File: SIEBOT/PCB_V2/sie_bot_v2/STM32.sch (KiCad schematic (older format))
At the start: 50 parts, among them P11 CONN_3X2, P12 CONN_3X2, P13 CONN_3X2, P14 CONN_3X2, P8 CONN_12X2, P9 CONN_12X2, Q2 BS170F, Q3 BS170F, Q4 BS170F, Q5 BS170F, Q6 BS170F, Q7 BS170F, Q8 BS170F, Q9 BS170F, U10 STM32F105RC, U11 LT1117CST-3.3, U12 ZXMHC3F381N8, U13 ZXMHC3F381N8, U14 ZXMHC3F381N8, U15 ZXMHC3F381N8, X3 8MHz

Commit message: Adición de ejemplos, modificación de los fuentes de elua para soportar el stm32f105
Cambios en el PCB para tener comunicación entre el IMX y el STM32 por puerto serial e i2c
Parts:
- removed P11, P12, P13, P14: CONN_3X2, pin_array_3x2, symbol CONN_3X2
- removed R26: 510, SM0603, symbol R
- added P?: CONN_5X2, pin_array_5x2, symbol CONN_5X2
- added R46: 150, SM0603, symbol R
- added R? (x2): 4.7k, SM0603, symbol R
- X3: value 8MHz -> 12MHz; footprint ABM3B -> ABM8G
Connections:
- net labels added: GMTR, STM_UART_RX, STM_UART_TX, VMTR
- net labels removed: GMTR1, GMTR2, GMTR3, GMTR4, VMTR1, VMTR2, VMTR3, VMTR4
- wire segments 266 -> 259
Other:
- note removed: "Boot mode select"
- note removed: "El procesador selecciona si inicia por \nla flash o ram internas.\nSe debe soldar solo R26 o R34\n\n"
- moved on the sheet: R34, R40, R41, R44, R45, U14, U15

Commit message: Inicio de ruteo de los cambios realizados en el esquematico
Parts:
- P6: renamed from P?; footprint pin_array_5x2 -> PIN_ARRAY_5x2
- gave numbers to parts that had none: 2
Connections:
- net labels added: TDO
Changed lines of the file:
@@
-EESchema Schematic File Version 2  date Fri 10 Feb 2012 05:02:18 PM COT
+EESchema Schematic File Version 2  date Fri 10 Feb 2012 06:23:52 PM COT
 LIBS:con-jack
 LIBS:adm3101e
@@
 STM_UART_RX
 $Comp
-L R R?
+L R R47
 U 1 1 4F352DAA
 P 2050 7200
-F 0 "R?" V 2130 7200 50  0000 C CNN
+F 0 "R47" V 2130 7200 50  0000 C CNN
 F 1 "4.7k" V 2050 7200 50  0000 C CNN
 F 2 "SM0603" H 2050 7200 60  0001 C CNN
@@
 $EndComp
 $Comp
-L R R?
+L R R26
 U 1 1 4F352D8D
 P 1900 7200
-F 0 "R?" V 1980 7200 50  0000 C CNN
+F 0 "R26" V 1980 7200 50  0000 C CNN
 F 1 "4.7k" V 1900 7200 50  0000 C CNN
 F 2 "SM0603" H 1900 7200 60  0001 C CNN
@@
 $EndComp
 $Comp
-L 3V3 #PWR?
+L 3V3 #PWR80
 U 1 1 4F352D37
 P 2050 6850
-F 0 "#PWR?" H 2050 6950 30  0001 C CNN
+F 0 "#PWR80" H 2050 6950 30  0001 C CNN
 F 1 "3V3" H 2050 6960 30  0000 C CNN
 	1    2050 6850
@@
 VMTR
 $Comp
-L CONN_5X2 P?
+L CONN_5X2 P6
 U 1 1 4F352742
 P 9050 6200
-F 0 "P?" H 9050 6500 60  0000 C CNN
+F 0 "P6" H 9050 6500 60  0000 C CNN
 F 1 "CONN_5X2" V 9050 6200 50  0000 C CNN
-F 2 "pin_array_5x2" H 9050 6200 60  0001 C CNN
+F 2 "PIN_ARRAY_5x2" H 9050 6200 60  0001 C CNN
 	1    9050 6200
 	1    0    0    -1
@@
 I2C1_SDA
 $Comp
-L 3V3 #PWR8
+L 3V3 #PWR86
 U 1 1 4E8A099D
 P 6050 8950
-F 0 "#PWR8" H 6050 9050 30  0001 C CNN
+F 0 "#PWR86" H 6050 9050 30  0001 C CNN
 F 1 "3V3" H 6050 9060 30  0000 C CNN
 	1    6050 8950
@@
 $EndComp
 $Comp
-L 3V3 #PWR3
+L 3V3 #PWR81
 U 1 1 4E8A0997
 P 3700 7900
-F 0 "#PWR3" H 3700 8000 30  0001 C CNN
+F 0 "#PWR81" H 3700 8000 30  0001 C CNN
 F 1 "3V3" H 3700 8010 30  0000 C CNN
 	1    3700 7900
@@
 $EndComp
 $Comp
-L 3V3 #PWR2
+L 3V3 #PWR79
 U 1 1 4E8A0992
 P 1500 7900
-F 0 "#PWR2" H 1500 8000 30  0001 C CNN
+F 0 "#PWR79" H 1500 8000 30  0001 C CNN
 F 1 "3V3" H 1500 8010 30  0000 C CNN
 	1    1500 7900
@@
 $EndComp
 $Comp
-L VDD5V #PWR9
+L VDD5V #PWR083
 U 1 1 4E7B5061
 P 6700 1000
-F 0 "#PWR9" H 6700 1100 30  0001 C CNN
+F 0 "#PWR083" H 6700 1100 30  0001 C CNN
 F 1 "VDD5V" H 6700 1100 30  0000 C CNN
 	1    6700 1000
@@
 $EndComp
 $Comp
-L GND #PWR10
+L GND #PWR084
 U 1 1 4E7B4E89
 P 6700 1650
-F 0 "#PWR10" H 6700 1650 30  0001 C CNN
+F 0 "#PWR084" H 6700 1650 30  0001 C CNN
 F 1 "GND" H 6700 1580 30  0001 C CNN
 	1    6700 1650
@@
 $EndComp
 $Comp
-L GND #PWR14
+L GND #PWR085
 U 1 1 4E7B4E84
 P 8150 1650
-F 0 "#PWR14" H 8150 1650 30  0001 C CNN
+F 0 "#PWR085" H 8150 1650 30  0001 C CNN
 F 1 "GND" H 8150 1580 30  0001 C CNN
 	1    8150 1650
@@
 $EndComp
 $Comp
-L GND #PWR12
+L GND #PWR086
 U 1 1 4E7B44BE
 P 7750 1650
-F 0 "#PWR12" H 7750 1650 30  0001 C CNN
+F 0 "#PWR086" H 7750 1650 30  0001 C CNN
 F 1 "GND" H 7750 1580 30  0001 C CNN
 	1    7750 1650
@@
 $EndComp
 $Comp
-L GND #PWR11
+L GND #PWR087
 U 1 1 4E7B44A2
 P 6900 1250
-F 0 "#PWR11" H 6900 1250 30  0001 C CNN
+F 0 "#PWR087" H 6900 1250 30  0001 C CNN
 F 1 "GND" H 6900 1180 30  0001 C CNN
 	1    6900 1250
@@
 $EndComp
 $Comp
-L 3V3 #PWR13
+L 3V3 #PWR91
 U 1 1 4E7B4482
 P 8150 900
-F 0 "#PWR13" H 8150 1000 30  0001 C CNN
+F 0 "#PWR91" H 8150 1000 30  0001 C CNN
 F 1 "3V3" H 8150 1010 30  0000 C CNN
 	1    8150 900
@@
 $EndComp
 $Comp
-L GND #PWR24
+L GND #PWR088
 U 1 1 4E78C5F4
 P 10800 2850
-F 0 "#PWR24" H 10800 2850 30  0001 C CNN
+F 0 "#PWR088" H 10800 2850 30  0001 C CNN
 F 1 "GND" H 10800 2780 30  0001 C CNN
 	1    10800 2850
@@
 $EndComp
 $Comp
-L 3V3 #PWR16
+L 3V3 #PWR94
 U 1 1 4E78C319
 P 8550 2150
-F 0 "#PWR16" H 8550 2250 30  0001 C CNN
+F 0 "#PWR94" H 8550 2250 30  0001 C CNN
 F 1 "3V3" H 8550 2260 30  0000 C CNN
 	1    8550 2150
@@
 $EndComp
 $Comp
-L GND #PWR7
+L GND #PWR089
 U 1 1 4E78C2ED
 P 5300 7400
-F 0 "#PWR7" H 5300 7400 30  0001 C CNN
+F 0 "#PWR089" H 5300 7400 30  0001 C CNN
 F 1 "GND" H 5300 7330 30  0001 C CNN
 	1    5300 7400
@@
 JTDI
 $Comp
-L 3V3 #PWR4
+L 3V3 #PWR82
 U 1 1 4E78BA06
 P 4150 1100
-F 0 "#PWR4" H 4150 1200 30  0001 C CNN
+F 0 "#PWR82" H 4150 1200 30  0001 C CNN
 F 1 "3V3" H 4150 1210 30  0000 C CNN
 	1    4150 1100
@@
 $EndComp
 $Comp
-L 3V3 #PWR15
+L 3V3 #PWR93
 U 1 1 4E2A2E11
 P 8350 2150
-F 0 "#PWR15" H 8350 2250 30  0001 C CNN
+F 0 "#PWR93" H 8350 2250 30  0001 C CNN
 F 1 "3V3" H 8350 2260 30  0000 C CNN
 	1    8350 2150
@@
 $EndComp
 $Comp
-L 3V3 #PWR18
+L 3V3 #PWR96
 U 1 1 4E2A2E03
 P 8750 1000
-F 0 "#PWR18" H 8750 1100 30  0001 C CNN
+F 0 "#PWR96" H 8750 1100 30  0001 C CNN
 F 1 "3V3" H 8750 1110 30  0000 C CNN
 	1    8750 1000
@@
 $EndComp
 $Comp
-L 3V3 #PWR6
+L 3V3 #PWR84
 U 1 1 4E2A2DF0
 P 4700 1150
-F 0 "#PWR6" H 4700 1250 30  0001 C CNN
+F 0 "#PWR84" H 4700 1250 30  0001 C CNN
 F 1 "3V3" H 4700 1260 30  0000 C CNN
 	1    4700 1150
@@
 $EndComp
 $Comp
-L GND #PWR22
+L GND #PWR090
 U 1 1 4E188E4E
 P 10550 1500
-F 0 "#PWR22" H 10550 1500 30  0001 C CNN
+F 0 "#PWR090" H 10550 1500 30  0001 C CNN
 F 1 "GND" H 10550 1430 30  0001 C CNN
 	1    10550 1500
@@
 FP1
 $Comp
-L GND #PWR19
+L GND #PWR091
 U 1 1 4E186DEB
 P 9250 1500
-F 0 "#PWR19" H 9250 1500 30  0001 C CNN
+F 0 "#PWR091" H 9250 1500 30  0001 C CNN
 F 1 "GND" H 9250 1430 30  0001 C CNN
 	1    9250 1500
@@
 JTRST
 Text Label 6100 6300 2    60   ~ 0
-JTDO
+TDO
 Text Label 6100 6200 2    60   ~ 0
 JTMS
@@
 $EndComp
 $Comp
-L GND #PWR17
+L GND #PWR092
 U 1 1 4E07869F
 P 8550 2800
-F 0 "#PWR17" H 8550 2800 30  0001 C CNN
+F 0 "#PWR092" H 8550 2800 30  0001 C CNN
 F 1 "GND" H 8550 2730 30  0001 C CNN
 	1    8550 2800
@@
 $EndComp
 $Comp
-L GND #PWR5
+L GND #PWR093
 U 1 1 4DCDB18D
 P 4300 7400
-F 0 "#PWR5" H 4300 7400 30  0001 C CNN
+F 0 "#PWR093" H 4300 7400 30  0001 C CNN
 F 1 "GND" H 4300 7330 30  0001 C CNN
 	1    4300 7400
@@
 $EndComp
 $Comp
-L GND #PWR20
+L GND #PWR094
 U 1 1 4DCDB183
 P 9650 2800
-F 0 "#PWR20" H 9650 2800 30  0001 C CNN
+F 0 "#PWR094" H 9650 2800 30  0001 C CNN
 F 1 "GND" H 9650 2730 30  0001 C CNN
 	1    9650 2800
@@
 NRST
 $Comp
-L GND #PWR1
+L GND #PWR095
 U 1 1 4DCDB180
 P 700 2050
-F 0 "#PWR1" H 700 2050 30  0001 C CNN
+F 0 "#PWR095" H 700 2050 30  0001 C CNN
 F 1 "GND" H 700 1980 30  0001 C CNN
 	1    700  2050
@@
 BOOT0
 $Comp
-L GND #PWR21
+L GND #PWR096
 U 1 1 4DCDB17D
 P 10400 2850
-F 0 "#PWR21" H 10400 2850 30  0001 C CNN
+F 0 "#PWR096" H 10400 2850 30  0001 C CNN
 F 1 "GND" H 10400 2780 30  0001 C CNN
 	1    10400 2850

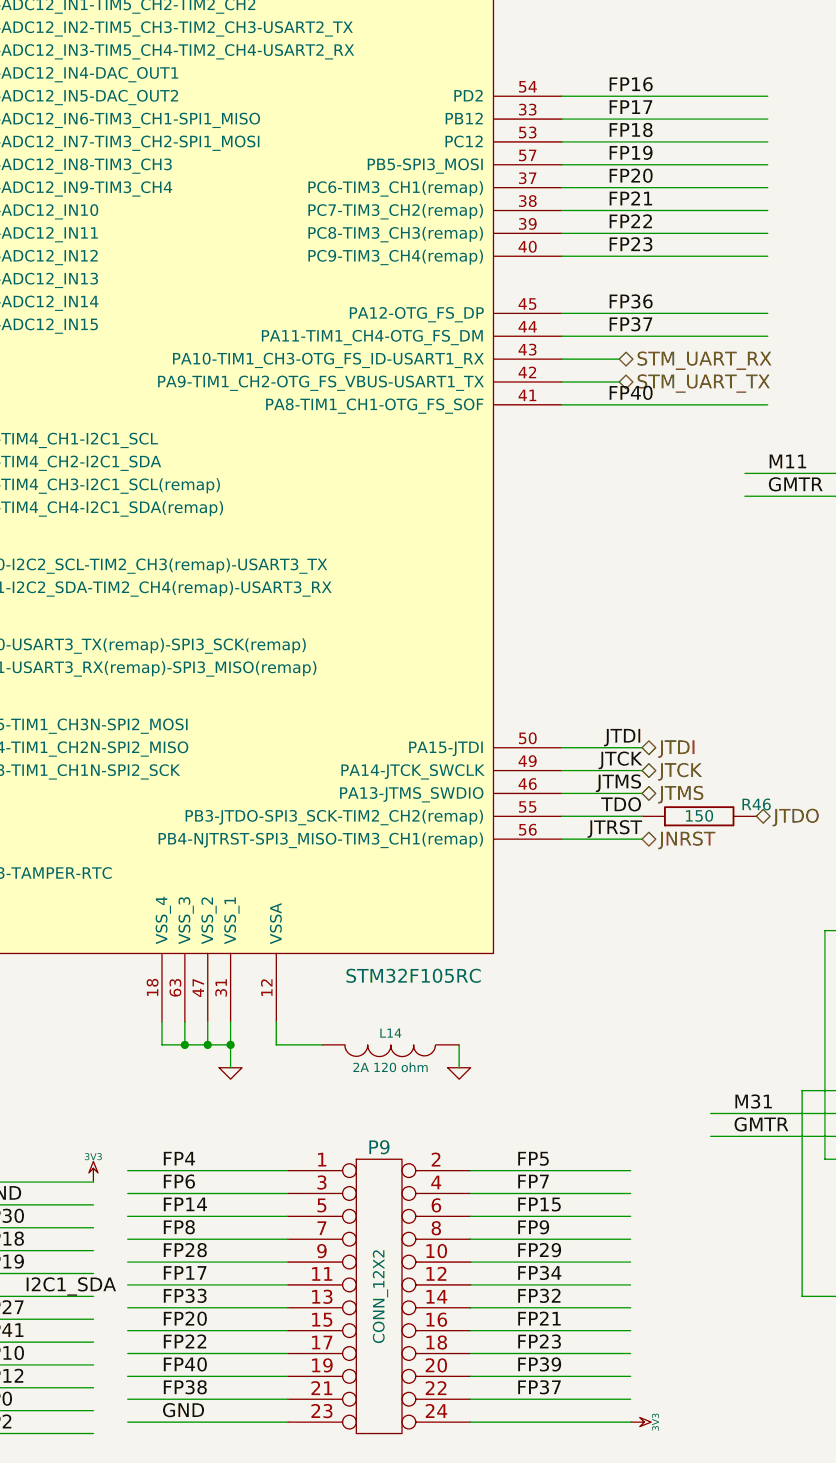
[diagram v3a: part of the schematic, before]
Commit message: Ruteo de las señales de control de los puente H 1, 3, 4
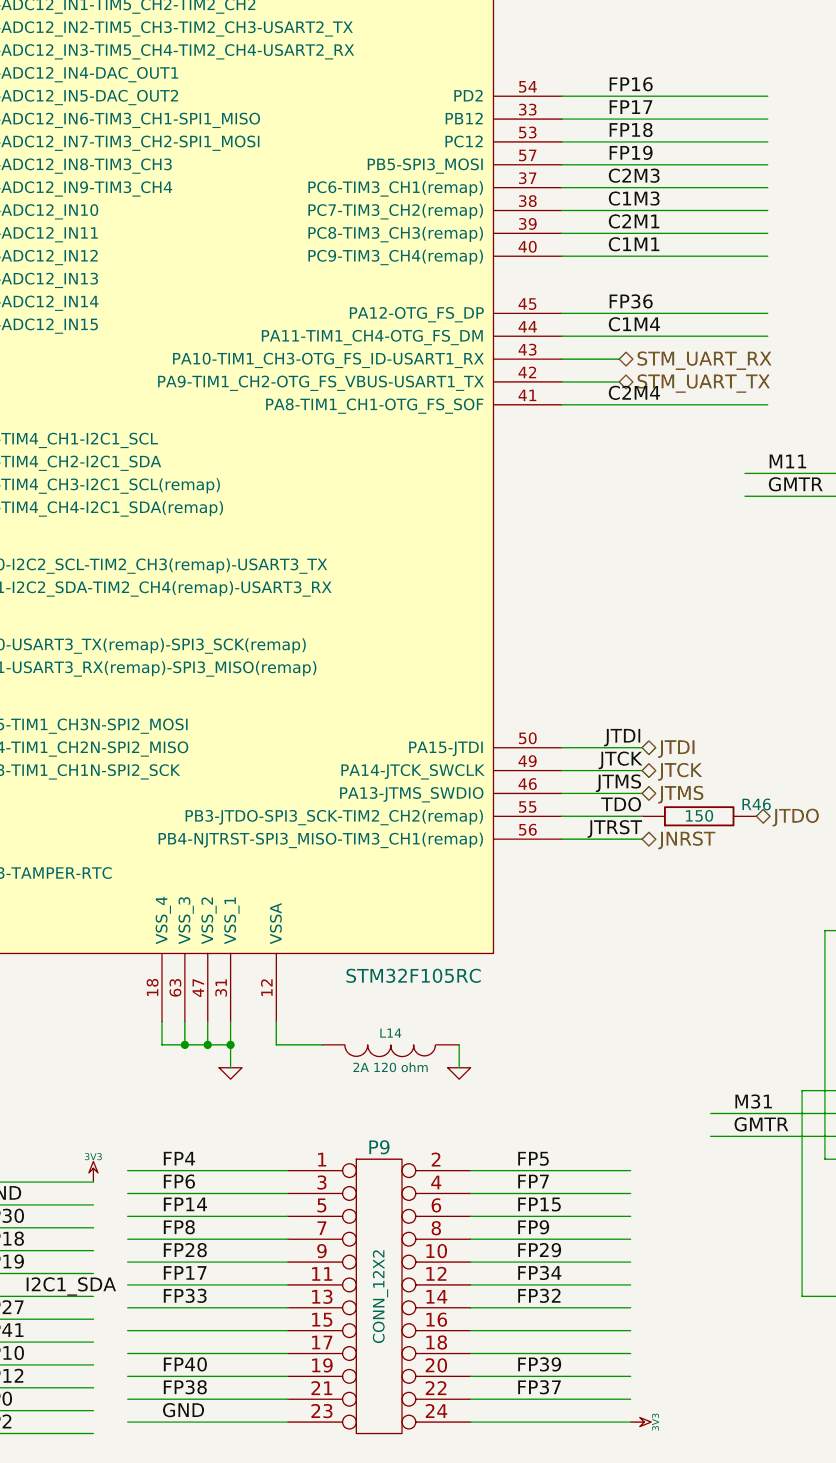
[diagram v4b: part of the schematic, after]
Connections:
- net labels removed: FP20, FP21, FP22, FP23
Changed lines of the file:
@@
-EESchema Schematic File Version 2  date Fri 10 Feb 2012 06:23:52 PM COT
+EESchema Schematic File Version 2  date Thu 16 Feb 2012 07:24:53 AM COT
 LIBS:con-jack
 LIBS:adm3101e
@@
 Sheet 3 5
 Title ""
-Date "10 feb 2012"
+Date "16 feb 2012"
 Rev ""
 Comp ""
@@
 Comment4 ""
 $EndDescr
+Text Label 5950 4500 0    60   ~ 0
+C2M4
+Text Label 5950 4200 0    60   ~ 0
+C1M4
+Text Label 5950 3850 0    60   ~ 0
+C1M1
+Text Label 5950 3750 0    60   ~ 0
+C2M1
+Text Label 5950 3650 0    60   ~ 0
+C1M3
+Text Label 5950 3550 0    60   ~ 0
+C2M3
+Wire Wire Line
+	5750 3750 6650 3750
 Wire Wire Line
 	6000 4400 5750 4400
@@
 Wire Wire Line
 	6650 3550 5750 3550
-Wire Wire Line
-	5750 3750 6650 3750
 Wire Wire Line
 	5750 3350 6650 3350
@@
 Text Label 4000 8850 0    60   ~ 0
 FP38
-Text Label 5550 8650 0    60   ~ 0
-FP23
 Text Label 5550 7850 0    60   ~ 0
 FP5
@@
 Text Label 5550 8450 0    60   ~ 0
 FP32
-Text Label 5550 8550 0    60   ~ 0
-FP21
 Text Label 4000 7950 0    60   ~ 0
 FP6
@@
 Text Label 4000 8450 0    60   ~ 0
 FP33
-Text Label 4000 8550 0    60   ~ 0
-FP20
-Text Label 4000 8650 0    60   ~ 0
-FP22
 Text Label 4000 8750 0    60   ~ 0
 FP40
@@
 Text Label 6000 2200 0    60   ~ 0
 FP41
-Text Label 5950 4500 0    60   ~ 0
-FP40
-Text Label 5950 4200 0    60   ~ 0
-FP37
 Text Label 5950 4100 0    60   ~ 0
 FP36
@@
 Text Label 1000 6550 0    60   ~ 0
 FP35
-Text Label 5950 3550 0    60   ~ 0
-FP20
-Text Label 5950 3650 0    60   ~ 0
-FP21
-Text Label 5950 3750 0    60   ~ 0
-FP22
-Text Label 5950 3850 0    60   ~ 0
-FP23
 Text Label 5950 3450 0    60   ~ 0
 FP19

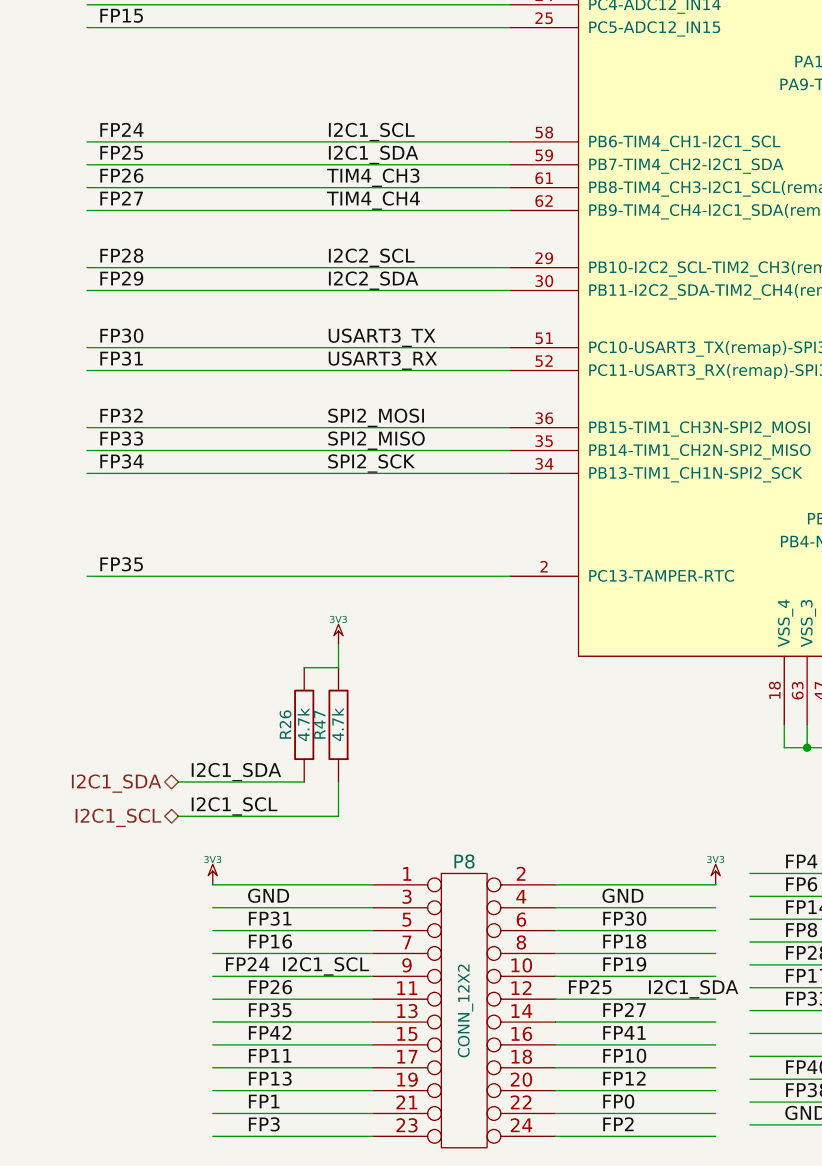
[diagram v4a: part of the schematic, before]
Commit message: Ruteo del último puente H
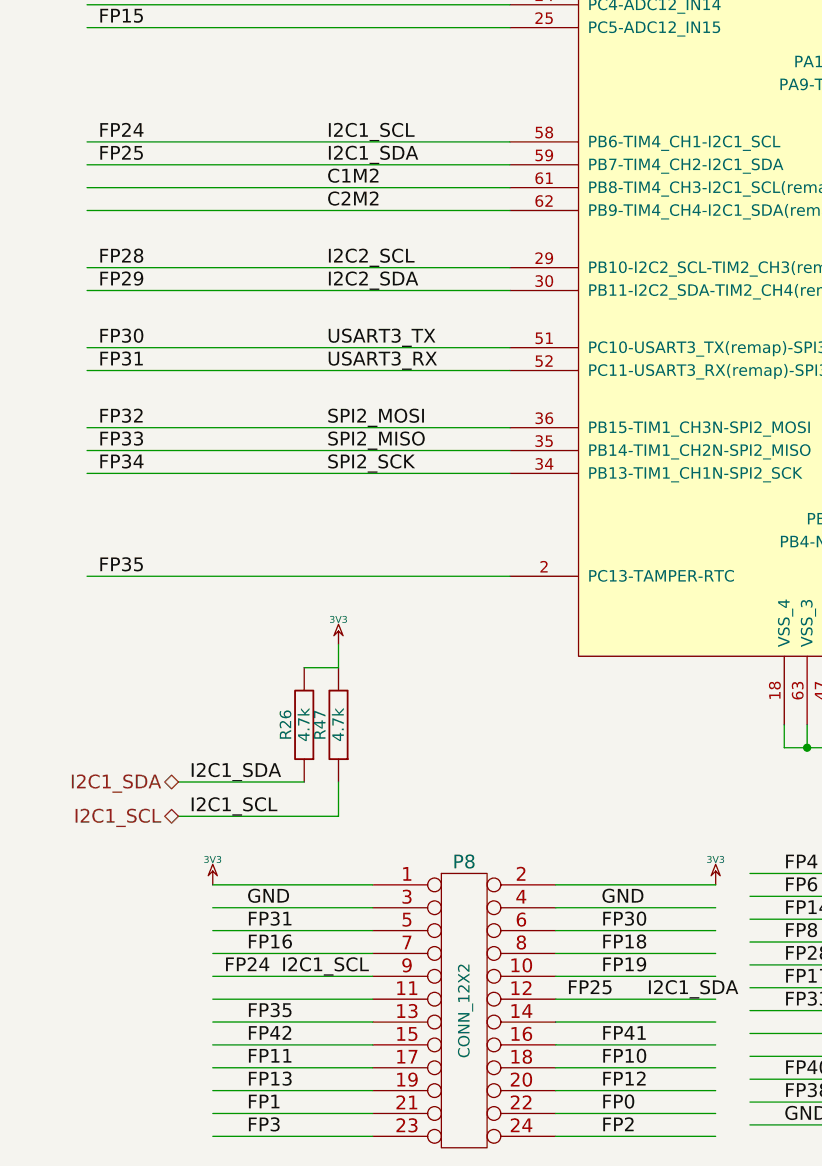
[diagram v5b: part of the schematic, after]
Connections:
- net labels removed: FP26, FP27, TIM4_CH3, TIM4_CH4
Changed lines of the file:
@@
-EESchema Schematic File Version 2  date Thu 16 Feb 2012 07:24:53 AM COT
+EESchema Schematic File Version 2  date Thu 16 Feb 2012 10:36:53 AM COT
 LIBS:con-jack
 LIBS:adm3101e
@@
 Text Label 3200 8600 0    60   ~ 0
 FP41
-Text Label 3200 8500 0    60   ~ 0
-FP27
 Text Label 3050 8400 0    60   ~ 0
 FP25
@@
 Text Label 1650 8500 0    60   ~ 0
 FP35
-Text Label 1650 8400 0    60   ~ 0
-FP26
 Text Label 1550 8300 0    60   ~ 0
 FP24
@@
 Text Label 1000 4750 0    60   ~ 0
 FP25
-Text Label 1000 4850 0    60   ~ 0
-FP26
-Text Label 1000 4950 0    60   ~ 0
-FP27
 Text Label 1000 5200 0    60   ~ 0
 FP28
@@
 TIM5_CH3
 Text Label 2000 4950 0    60   ~ 0
-TIM4_CH4
+C2M2
 Text Label 2000 4850 0    60   ~ 0
-TIM4_CH3
+C1M2
 Text Label 1650 3550 0    60   ~ 0
 TIM3_CH4
